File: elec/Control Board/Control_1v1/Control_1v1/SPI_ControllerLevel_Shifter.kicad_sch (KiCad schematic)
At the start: 34 parts, among them J301 RJ12_6P6C_HORZ, J302 0.100_2Pin, Q301 BSS138, Q302 BSS138, Q303 BSS138, Q304 BSS138

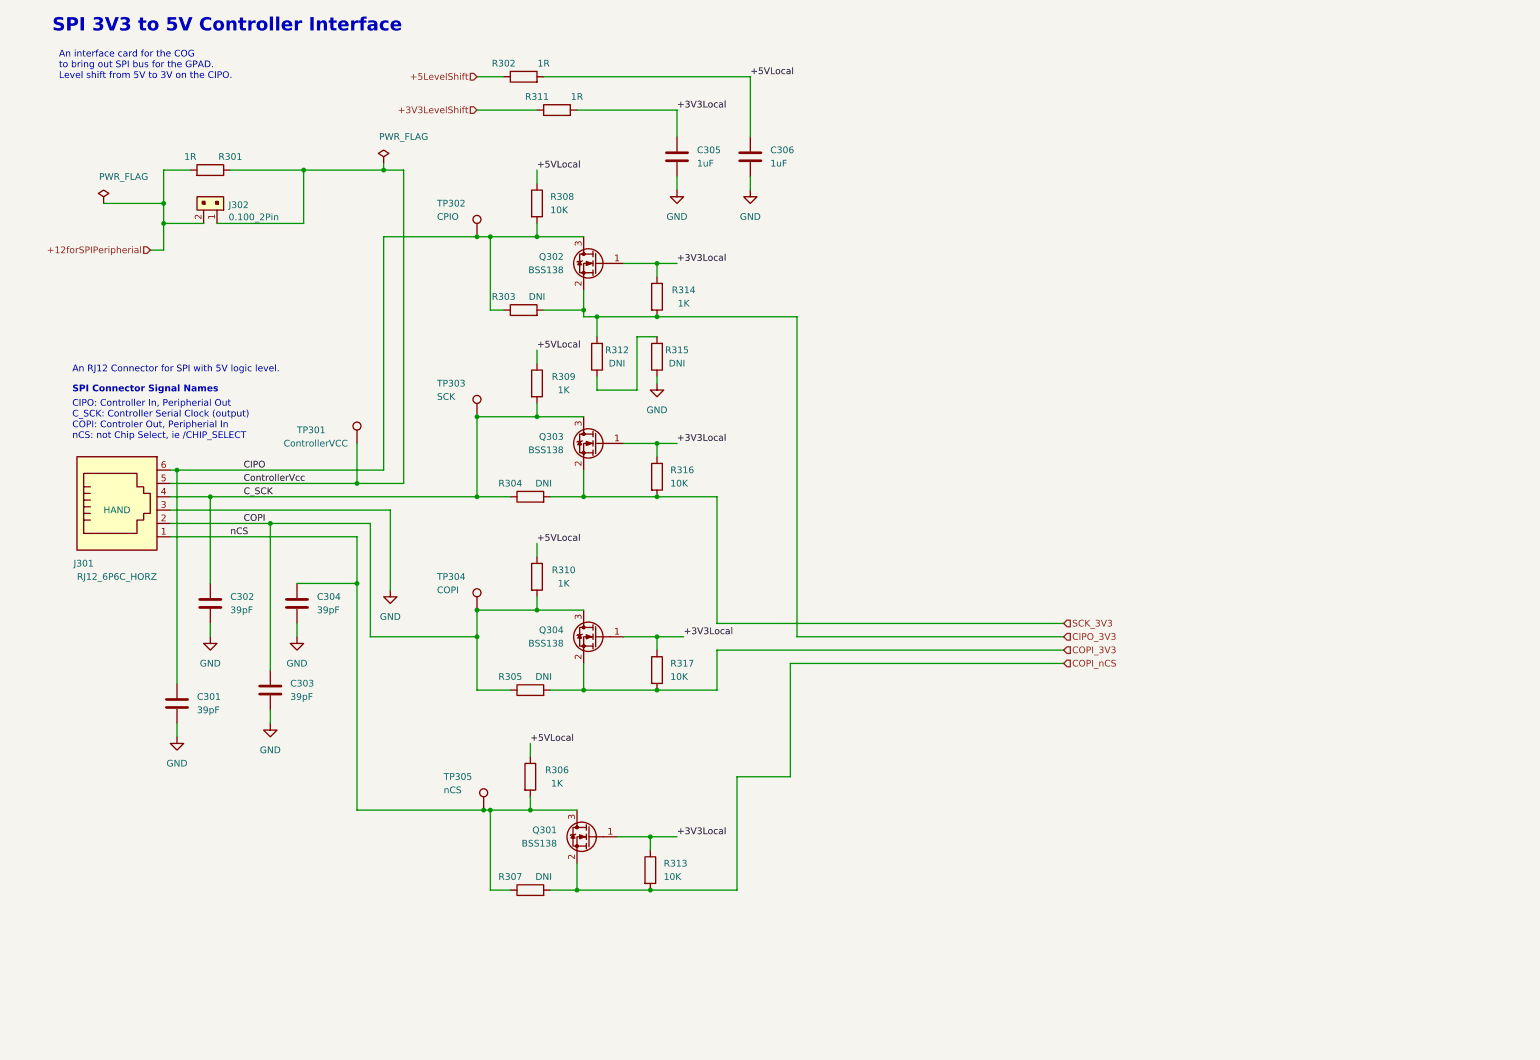
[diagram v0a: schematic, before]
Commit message: Add sheet with title block.
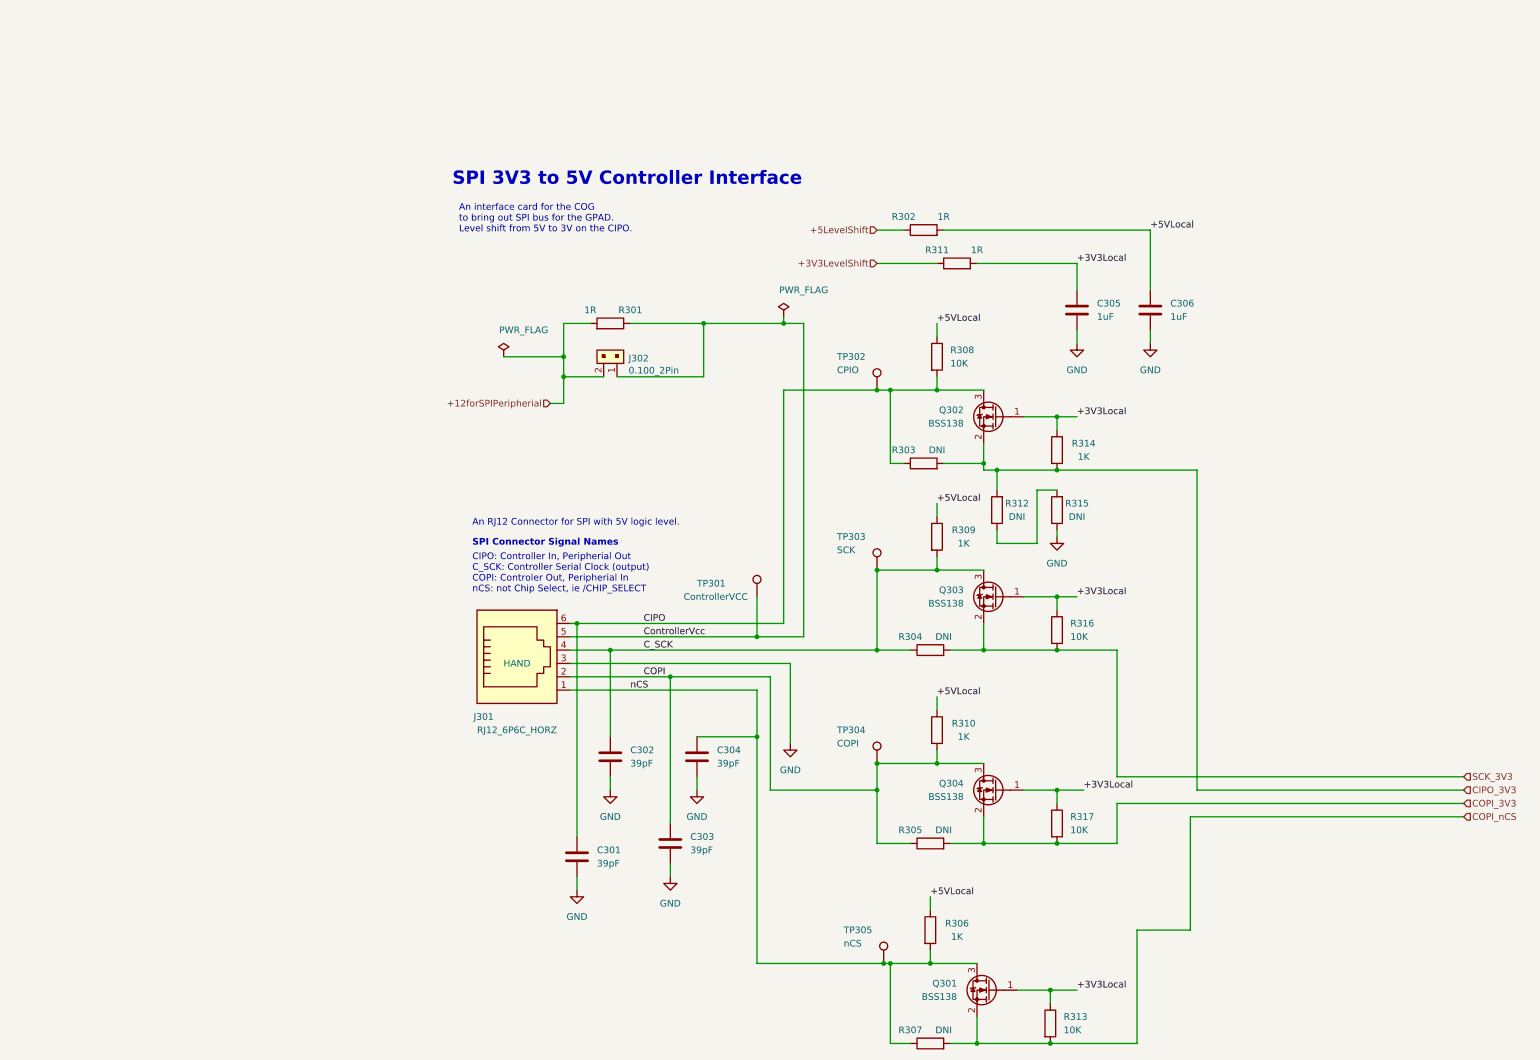
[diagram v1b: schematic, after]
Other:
- company: (none) -> Public Invention
- title: (none) -> Control Interconnect Board
- moved on the sheet: C301, C302, C303, C304, C305, C306, J301, J302, Q301, Q302, Q303, Q304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

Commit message: Fix J10 backwards.
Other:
- title: Control Interconnect Board -> Control Interconnect Board OEDCS
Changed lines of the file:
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@@
   (paper "USLedger")
   (title_block
-    (title "Control Interconnect Board")
+    (title "Control Interconnect Board OEDCS")
     (date "2023-10-10")
     (rev "Rev 1.1")
     (company "Public Invention")
-    (comment 1 "Contributor: Lawrence Kinceloe")
+    (comment 1 "GNU Affero General Public License v3.0")
+    (comment 2 "Contributor: Lawrence Kinceloe")
+    (comment 3 "Drawn By: (Forrest) Lee Erickson")
   )
   (junction (at 187.96 194.31) (diameter 0) (color 0 0 0 0)

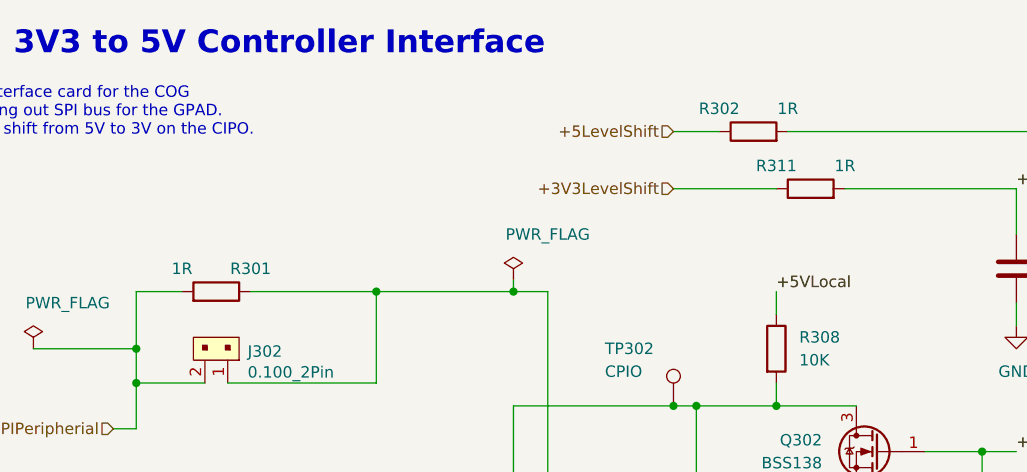
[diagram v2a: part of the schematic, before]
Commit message: Add power shutdown button. Add thermocouple ground screw terminals. Isolate SCL from SDA traces. Make first cut BOM.
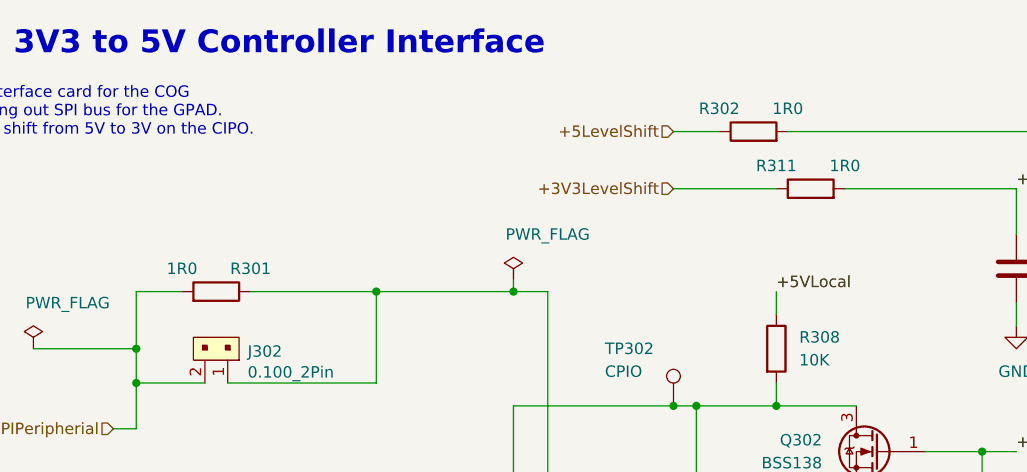
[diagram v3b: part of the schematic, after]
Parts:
- R301, R302, R311: value 1R -> 1R0; Distributor 1 NA -> JLCPCB; Distributor 1 PN NA -> C269434; MPN (none) -> RMC060315%N; Manufacturer (none) -> TyoHM
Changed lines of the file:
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@@
       (effects (font (size 1.27 1.27)))
     )
-    (property "Value" "1R" (at 130.81 69.85 90)
+    (property "Value" "1R0" (at 130.81 69.85 90)
       (effects (font (size 1.27 1.27)))
     )
@@
       (effects (font (size 1.27 1.27)) hide)
     )
-    (property "Distributor 1" "NA" (at 134.62 72.39 0)
-      (effects (font (size 1.27 1.27)) hide)
-    )
-    (property "Distributor 1 PN" "NA" (at 134.62 72.39 0)
+    (property "Distributor 1" "JLCPCB" (at 134.62 72.39 0)
+      (effects (font (size 1.27 1.27)) hide)
+    )
+    (property "Distributor 1 PN" "C269434" (at 134.62 72.39 0)
       (effects (font (size 1.27 1.27)) hide)
     )
@@
       (effects (font (size 1.27 1.27)) hide)
     )
-    (property "Description" "Do Not Insert" (at 134.62 72.39 0)
+    (property "Description" "0.1W ±5% 1Ω 0603 Chip Resistor - Surface Mount ROHS" (at 134.62 72.39 0)
+      (effects (font (size 1.27 1.27)) hide)
+    )
+    (property "MPN" "RMC060315%N" (at 134.62 72.39 0)
+      (effects (font (size 1.27 1.27)) hide)
+    )
+    (property "Manufacturer" "TyoHM" (at 134.62 72.39 0)
       (effects (font (size 1.27 1.27)) hide)
     )
@@
       (effects (font (size 1.27 1.27)))
     )
-    (property "Value" "1R" (at 198.12 52.07 90)
+    (property "Value" "1R0" (at 198.12 52.07 90)
       (effects (font (size 1.27 1.27)))
     )
@@
       (effects (font (size 1.27 1.27)) hide)
     )
-    (property "Distributor 1" "NA" (at 194.31 54.61 0)
-      (effects (font (size 1.27 1.27)) hide)
-    )
-    (property "Distributor 1 PN" "NA" (at 194.31 54.61 0)
+    (property "Distributor 1" "JLCPCB" (at 194.31 54.61 0)
+      (effects (font (size 1.27 1.27)) hide)
+    )
+    (property "Distributor 1 PN" "C269434" (at 194.31 54.61 0)
       (effects (font (size 1.27 1.27)) hide)
     )
@@
       (effects (font (size 1.27 1.27)) hide)
     )
-    (property "Description" "Do Not Insert" (at 194.31 54.61 0)
+    (property "Description" "0.1W ±5% 1Ω 0603 Chip Resistor - Surface Mount ROHS" (at 194.31 54.61 0)
+      (effects (font (size 1.27 1.27)) hide)
+    )
+    (property "MPN" "RMC060315%N" (at 194.31 54.61 0)
+      (effects (font (size 1.27 1.27)) hide)
+    )
+    (property "Manufacturer" "TyoHM" (at 194.31 54.61 0)
       (effects (font (size 1.27 1.27)) hide)
     )
@@
       (effects (font (size 1.27 1.27)))
     )
-    (property "Value" "1R" (at 204.47 58.42 90)
+    (property "Value" "1R0" (at 204.47 58.42 90)
       (effects (font (size 1.27 1.27)))
     )
@@
       (effects (font (size 1.27 1.27)) hide)
     )
-    (property "Distributor 1" "NA" (at 200.66 60.96 0)
-      (effects (font (size 1.27 1.27)) hide)
-    )
-    (property "Distributor 1 PN" "NA" (at 200.66 60.96 0)
+    (property "Distributor 1" "JLCPCB" (at 200.66 60.96 0)
+      (effects (font (size 1.27 1.27)) hide)
+    )
+    (property "Distributor 1 PN" "C269434" (at 200.66 60.96 0)
       (effects (font (size 1.27 1.27)) hide)
     )
@@
       (effects (font (size 1.27 1.27)) hide)
     )
-    (property "Description" "Do Not Insert" (at 200.66 60.96 0)
-      (effects (font (size 1.27 1.27)) hide)
-    )
+    (property "Description" "0.1W ±5% 1Ω 0603 Chip Resistor - Surface Mount ROHS" (at 200.66 60.96 0)
+      (effects (font (size 1.27 1.27)) hide)
+    )
+    (property "MPN" "RMC060315%N" (at 200.66 60.96 0)
+      (effects (font (size 1.27 1.27)) hide)
+    )
+    (property "Manufacturer" "TyoHM" (at 200.66 60.96 0)
+      (effects (font (size 1.27 1.27)) hide)
+    )
